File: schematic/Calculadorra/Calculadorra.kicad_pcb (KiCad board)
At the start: 2 copper layers, 20 parts, among them SW1 SW_Push, SW10 SW_Push, SW11 SW_Push, SW12 SW_Push, SW13 SW_Push, SW14 SW_Push, SW15 SW_Push, SW16 SW_Push, SW2 SW_Push, SW3 SW_Push, SW4 SW_Push, SW5 SW_Push, SW6 SW_Push, SW7 SW_Push, SW8 SW_Push, SW9 SW_Push, U1 ATmega328-P, U2 LCD-016N002L

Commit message: No idea what changed
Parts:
- added B_(1: SW_Push, Button_Switch_Keyboard:SW_Cherry_MX_1.00u_PCB, F.Cu at (9.59, 17.1)
- added B_)1: SW_Push, Button_Switch_Keyboard:SW_Cherry_MX_1.00u_PCB, F.Cu at (9.59, 32.1)
- added B_0: SW_Push, Button_Switch_Keyboard:SW_Cherry_MX_1.00u_PCB, F.Cu at (9.59, 1.97)
- added B_=1: SW_Push, Button_Switch_Keyboard:SW_Cherry_MX_1.00u_PCB, F.Cu at (9.59, 47.2)
- moved U1 105.2 mm to (197.5, 88.7)
- moved RV1 96.2 mm to (112.7, 92.0)
- moved R1 88.8 mm to (127.5, 90.5)
- moved B_1 50.5 mm to (148.8, 105.0)
- moved B_4 36.1 mm to (123.5, 104.4)
- moved U2 32.0 mm to (133.0, 42.5)
- moved B_2 30.7 mm to (132.0, 127.4)
- moved B_3 29.6 mm to (131.5, 148.4)
- moved B_7 23.5 mm to (96.8, 104.0)
- moved B_Shift1 20.7 mm to (68.3, 103.5)
- moved B_6 15.0 mm to (105.0, 154.4)
- moved B_5 13.0 mm to (105.5, 130.0)
- moved B_Right1 12.9 mm to (61.1, 152.4)
- moved B_Left1 10.1 mm to (62.1, 131.4)
- moved B_9 6.32 mm to (83.5, 151.4)
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- renumbered SW13 to B_1, SW14 to B_2, SW15 to B_3, SW9 to B_4, SW10 to B_5, SW11 to B_6, SW5 to B_7, SW6 to B_8, SW7 to B_9, SW16 to B_Add1, SW2 to B_Left1, SW8 to B_Mul1, SW4 to B_On1, SW3 to B_Right1, SW1 to B_Shift1, SW12 to B_Sub1
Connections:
- B_1 pad 1: Net-(U1-PD3) -> Net-(U1-PD2)
- B_2 pad 1: Net-(U1-PD3) -> Net-(U1-PD2)
- B_3 pad 1: Net-(U1-PD3) -> Net-(U1-PD2)
- B_4 pad 1: Net-(U1-PD2) -> Net-(U1-PD1)
- B_5 pad 1: Net-(U1-PD2) -> Net-(U1-PD1)
- B_6 pad 1: Net-(U1-PD2) -> Net-(U1-PD1)
- B_7 pad 1: Net-(U1-PD1) -> Net-(U1-PD0)
- B_8 pad 1: Net-(U1-PD1) -> Net-(U1-PD0)
- B_9 pad 1: Net-(U1-PD1) -> Net-(U1-PD0)
- B_Add1 pad 1: Net-(U1-PD3) -> Net-(U1-PD2)
- B_Left1 pad 1: Net-(U1-PD0) -> Net-(U1-PC5)
- B_Mul1 pad 1: Net-(U1-PD1) -> Net-(U1-PD0)
- B_On1 pad 1: Net-(U1-PD0) -> Net-(U1-PC5)
- B_Right1 pad 1: Net-(U1-PD0) -> Net-(U1-PC5)
- B_Shift1 pad 1: Net-(U1-PD0) -> Net-(U1-PC5)
- B_Sub1 pad 1: Net-(U1-PD2) -> Net-(U1-PD1)
- U1 pad 28: unconnected-(U1-PC5-Pad28) -> Net-(U1-PC5)
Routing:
- net Net-(U1-PD4): track 45.4 -> 18.6 mm
- net Net-(U1-PD0): track 0.00 -> 26.7 mm

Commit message: Disseny de la PCB i model 3D fet durant la Hacknight
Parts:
- removed U2: LCD-016N002L, Display:LCD-016N002L
- added DS1: WC1602A, Display:WC1602A, F.Cu at (56.6, 31.6)
- moved B_0 160.3 mm to (62.0, 153.5)
- moved U1 159.7 mm to (52.0, 22.8), turned to 90 degrees
- moved B_(1 154.2 mm to (81.5, 153.5)
- moved B_=1 153.6 mm to (120.5, 153.5)
- moved B_)1 151.9 mm to (101.0, 153.5)
- moved B_On1 117.5 mm to (120.5, 73.5)
- moved B_1 91.4 mm to (62.0, 133.5)
- moved B_Mul1 91.1 mm to (120.5, 93.5)
- moved B_Right1 88.4 mm to (101.0, 73.5)
- moved R1 75.9 mm to (100.2, 19.6)
- moved RV1 73.2 mm to (119.2, 19.1)
- moved B_Sub1 69.8 mm to (120.5, 113.5)
- moved B_4 62.2 mm to (62.0, 113.5)
- moved B_Left1 61.1 mm to (81.5, 73.5)
- moved B_9 60.5 mm to (101.0, 93.5)
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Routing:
- net Net-(U1-PD3): track 0.00 -> 225.2 mm
- net Net-(U1-PD2): track 0.00 -> 201.7 mm
- net Net-(U1-PD1): track 0.00 -> 178.1 mm
- net Net-(U1-PD7): track 0.00 -> 146.4 mm
- net Net-(U1-PD0): track 26.7 -> 154.6 mm
- net Net-(U1-PC5): track 0.00 -> 121.9 mm
- net Net-(U1-PD4): track 18.6 -> 137.0 mm
- net VCC: track 0.00 -> 100.6 mm
- net Net-(U1-PD6): track 43.5 -> 139.3 mm
- net Net-(U1-PD5): track 47.0 -> 135.0 mm
- net GND: track 0.00 -> 83.2 mm
- net Net-(DS1-VO): track 0.00 -> 68.3 mm
- net Net-(DS1-D7): track 0.00 -> 32.3 mm
- net Net-(DS1-RS): track 0.00 -> 28.1 mm
- net Net-(DS1-D6): track 0.00 -> 28.0 mm
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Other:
- copper layers 2 -> 4

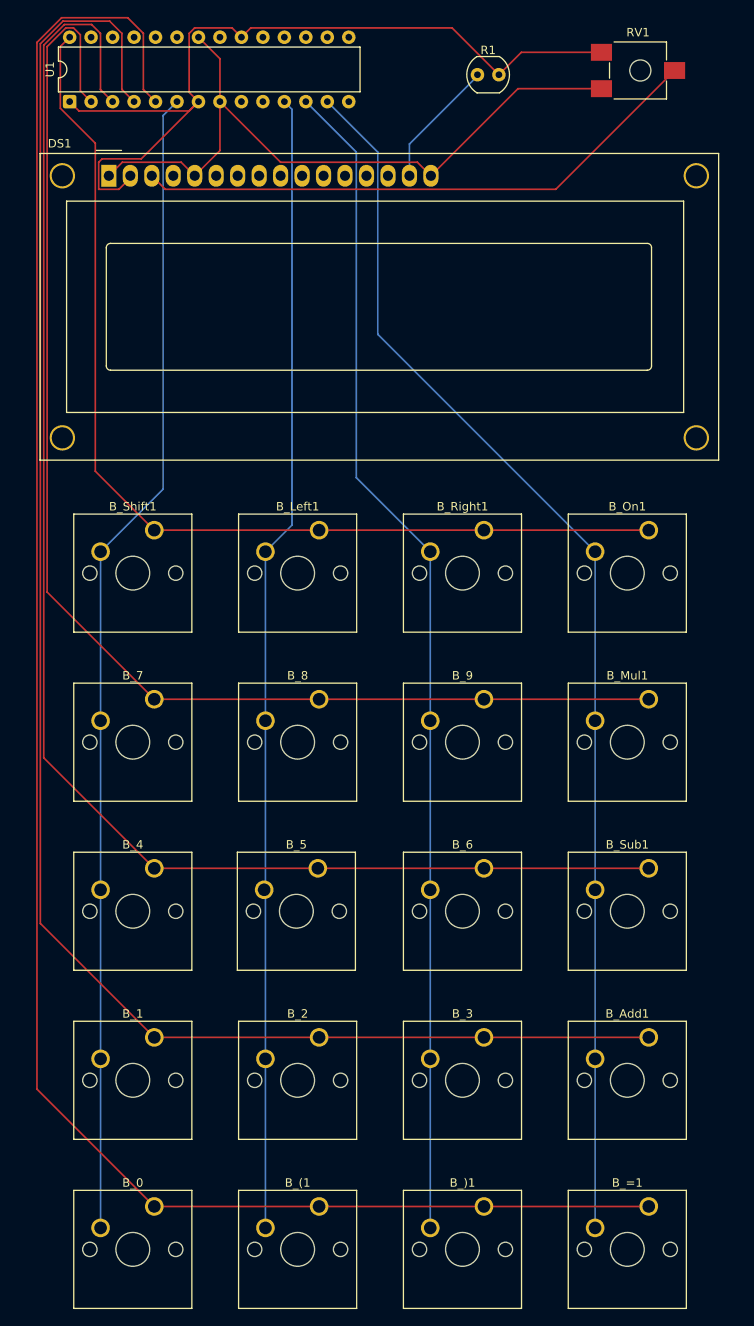
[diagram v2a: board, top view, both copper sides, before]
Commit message: PCB amb nous botons, ja posarem díodes i cables en altres moments
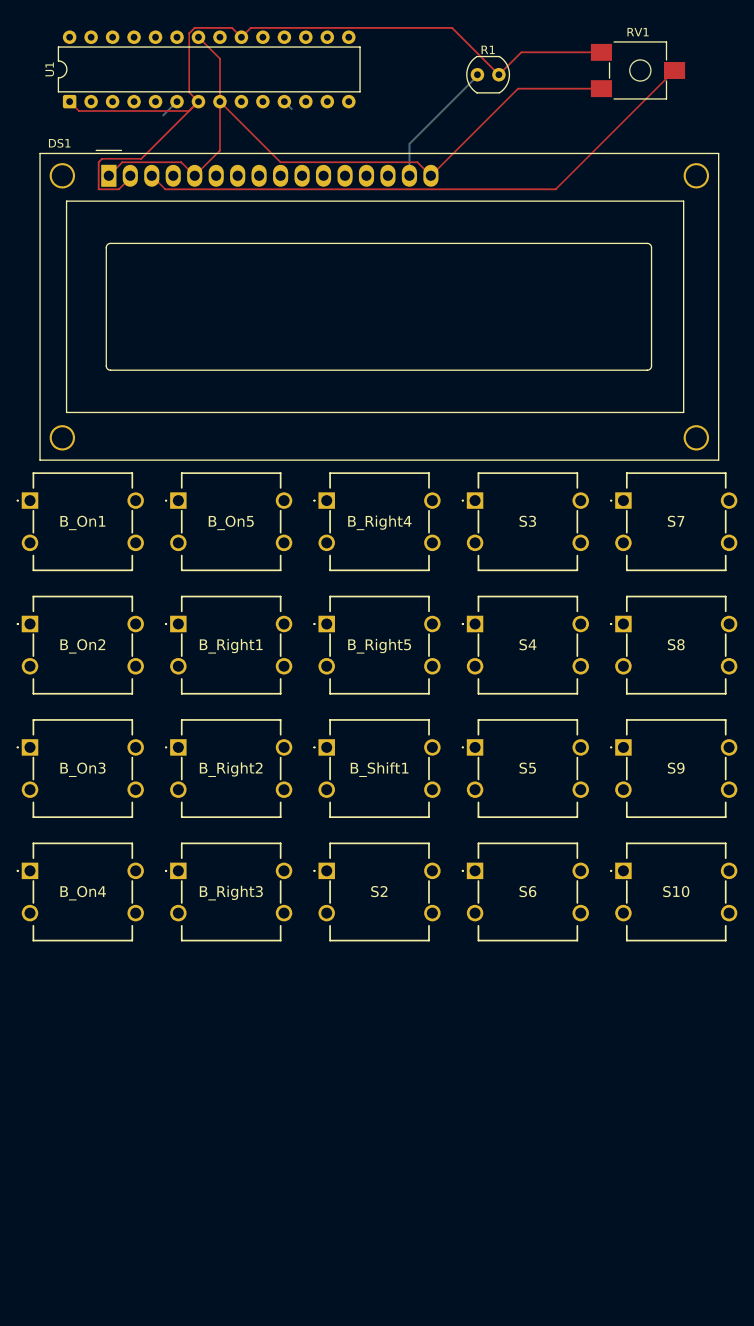
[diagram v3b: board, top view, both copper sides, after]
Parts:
- removed B_(1, B_)1, B_0, B_1, B_2, B_3, B_4, B_5, B_6, B_7, B_8, B_9, B_=1, B_Add1, B_Left1, B_Mul1, B_Sub1: SW_Push, Button_Switch_Keyboard:SW_Cherry_MX_1.00u_PCB
- added B_On2: COM-10302, Library:Button_COM10302, F.Cu at (47.3, 84.6)
- added B_On3: COM-10302, Library:Button_COM10302, F.Cu at (47.3, 99.2)
- added B_On4: COM-10302, Library:Button_COM10302, F.Cu at (47.3, 113.8)
- added B_On5: COM-10302, Library:Button_COM10302, F.Cu at (64.8, 70.0)
- added B_Right2: COM-10302, Library:Button_COM10302, F.Cu at (64.8, 99.2)
- added B_Right3: COM-10302, Library:Button_COM10302, F.Cu at (64.8, 113.8)
- added B_Right4: COM-10302, Library:Button_COM10302, F.Cu at (82.4, 70.0)
- added B_Right5: COM-10302, Library:Button_COM10302, F.Cu at (82.4, 84.6)
- added S10: COM-10302, Library:Button_COM10302, F.Cu at (117.5, 113.8)
- added S2: COM-10302, Library:Button_COM10302, F.Cu at (82.4, 113.8)
- added S3: COM-10302, Library:Button_COM10302, F.Cu at (100.0, 70.0)
- added S4: COM-10302, Library:Button_COM10302, F.Cu at (100.0, 84.6)
- added S5: COM-10302, Library:Button_COM10302, F.Cu at (100.0, 99.2)
- added S6: COM-10302, Library:Button_COM10302, F.Cu at (100.0, 113.8)
- added S7: COM-10302, Library:Button_COM10302, F.Cu at (117.5, 70.0)
- added S8: COM-10302, Library:Button_COM10302, F.Cu at (117.5, 84.6)
- added S9: COM-10302, Library:Button_COM10302, F.Cu at (117.5, 99.2)
- B_On1, B_Right1, B_Shift1: value SW_Push -> COM-10302; footprint Button_Switch_Keyboard:SW_Cherry_MX_1.00u_PCB -> Library:Button_COM10302
- moved B_On1 73.3 mm to (47.3, 70.0)
- moved B_Right1 37.8 mm to (64.8, 84.6)
- moved B_Shift1 32.8 mm to (82.4, 99.2)
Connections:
- B_On1 pad 1: Net-(U1-PC5) -> unconnected-(B_On1-COM_1-Pad1)
- B_Right1 pad 1: Net-(U1-PC5) -> unconnected-(B_Right1-COM_1-Pad1)
- B_Shift1 pad 1: Net-(U1-PC5) -> unconnected-(B_Shift1-COM_1-Pad1)
- U1 pad 28: Net-(U1-PC5) -> Net-(B_On1-NO_1)
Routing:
- net Net-(B_On5-NO_1): track 225.2 -> 0.00 mm
- net Net-(B_On4-NO_1): track 201.7 -> 0.00 mm
- net Net-(B_On3-NO_1): track 178.1 -> 0.00 mm
- net Net-(B_On2-NO_1): track 154.6 -> 0.00 mm
- net Net-(B_On1-COM_2): track 146.4 -> 0.00 mm
- net Net-(B_Right1-COM_2): track 139.3 -> 0.00 mm
- net Net-(B_Shift1-COM_2): track 137.0 -> 2.33 mm
- net Net-(S10-COM_2): track 135.0 -> 1.26 mm
- net Net-(U1-PC5): track 121.9 -> 0.00 mm
